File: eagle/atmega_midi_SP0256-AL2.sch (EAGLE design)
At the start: 40 parts, among them IC1 LTC6904, IC2 TL071P, U1 6N138, U2 ATMEGA328P_PDIP, U3 SP0256-AL2

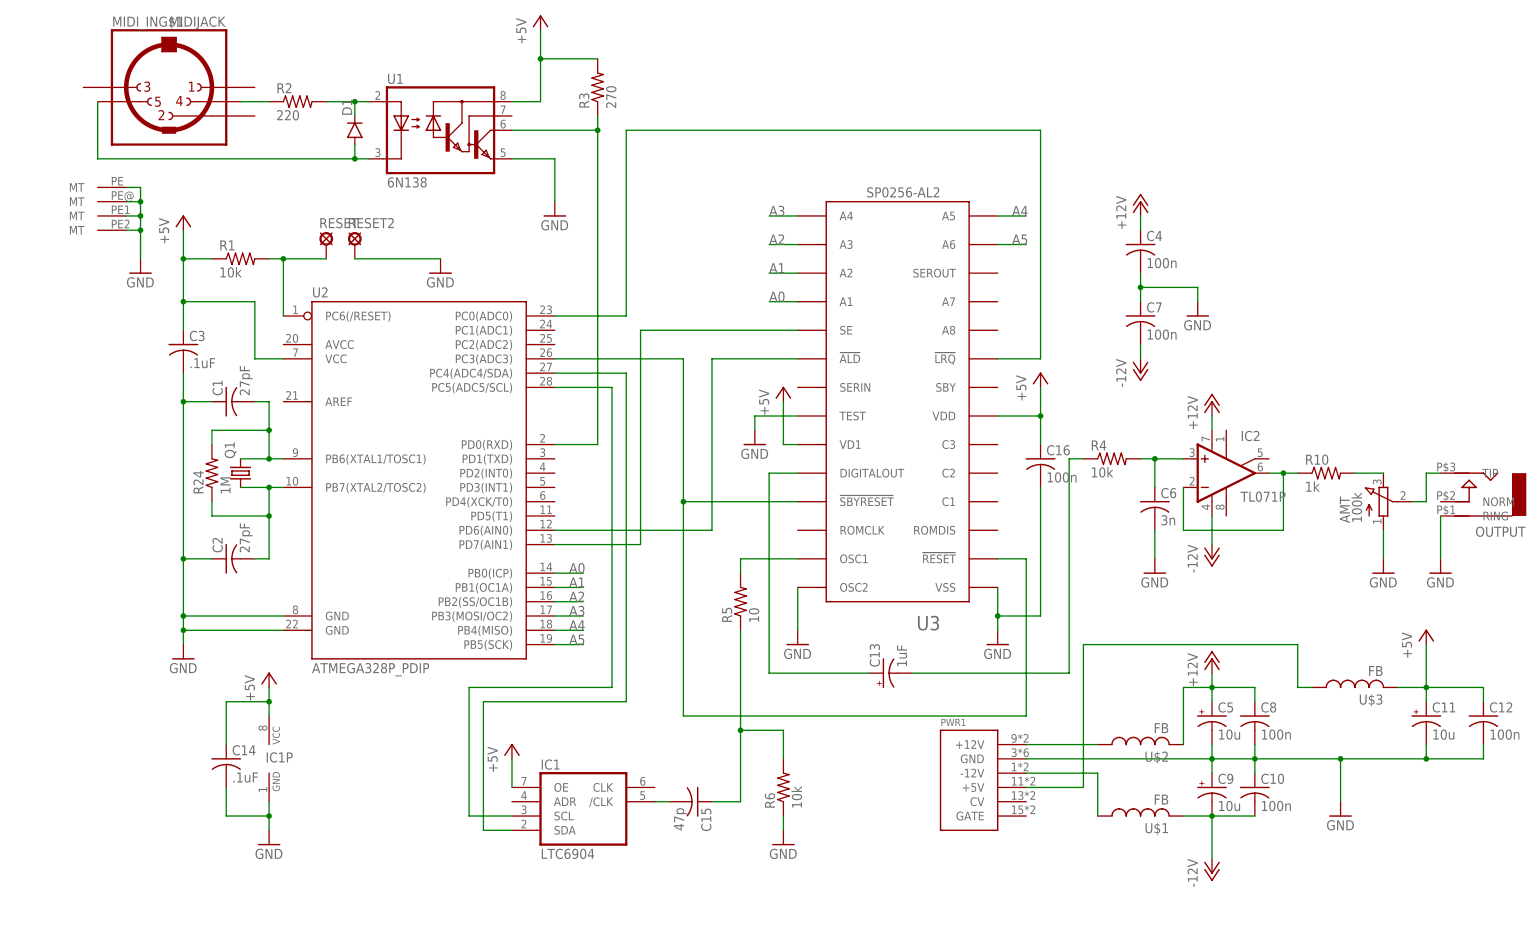
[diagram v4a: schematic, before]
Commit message: routed and stub code for pitch oscillator
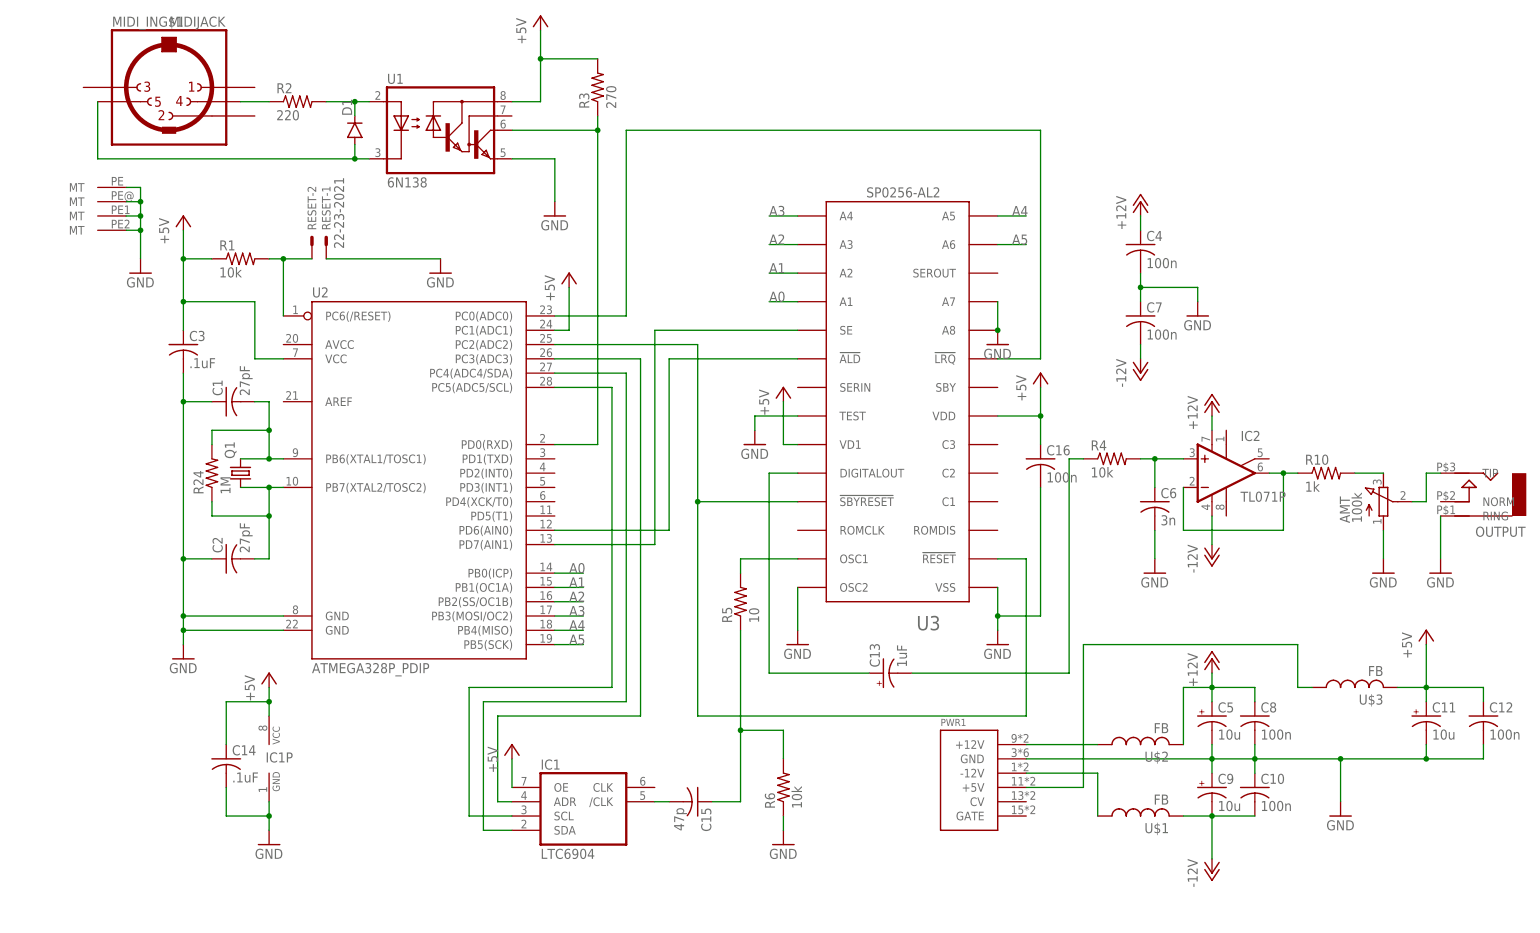
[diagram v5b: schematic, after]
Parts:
- removed RESET2: LSP11, solpad:LSP11
- C13: device rcl:CPOL-USB45181A -> rcl:CPOL-USE15-6AXIAL
- RESET: value LSP11 -> 22-23-2021; device solpad:LSP11 -> con-molex:22-23-2021
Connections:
- new net N$19: IC1G$1.ADR, U2.PC3(ADC3)
- net +5V: now also U2.PC1(ADC1)
- net GND: now also RESET-1.S, U3.A7, U3.A8; no longer RESET2.MP
- net N$1: now also U2.PC2(ADC2); no longer U2.PC3(ADC3)
- net N$43: now also RESET-2.S; no longer RESET.MP
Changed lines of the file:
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@@
 <part name="MIDI_IN" library="adafruit" deviceset="MIDIJACK" device=""/>
 <part name="U3" library="speech" deviceset="SP0256-AL2" device=""/>
-<part name="C13" library="rcl" deviceset="CPOL-US" device="B45181A" value="1uF"/>
+<part name="C13" library="rcl" deviceset="CPOL-US" device="E15-6AXIAL" value="1uF"/>
 <part name="P+3" library="supply1" deviceset="+5V" device=""/>
 <part name="P+6" library="supply1" deviceset="+5V" device=""/>
-<part name="RESET" library="solpad" deviceset="LSP11" device=""/>
-<part name="RESET2" library="solpad" deviceset="LSP11" device=""/>
 <part name="GND12" library="supply1" deviceset="GND" device=""/>
 <part name="GND11" library="supply1" deviceset="GND" device=""/>
@@
 <part name="R6" library="rcl" deviceset="R-US_" device="0207/7" value="10k"/>
 <part name="GND6" library="supply1" deviceset="GND" device=""/>
+<part name="GND10" library="supply1" deviceset="GND" device=""/>
+<part name="P+11" library="supply1" deviceset="+5V" device=""/>
+<part name="RESET" library="con-molex" deviceset="22-23-2021" device=""/>
 </parts>
 <sheets>
@@
 <instance part="P+3" gate="1" x="127" y="63.5"/>
 <instance part="P+6" gate="1" x="81.28" y="60.96"/>
-<instance part="RESET" gate="1" x="0" y="86.36"/>
-<instance part="RESET2" gate="1" x="5.08" y="86.36"/>
 <instance part="MIDI_IN" gate="G$2" x="-35.56" y="96.52" rot="R180"/>
 <instance part="MIDI_IN" gate="G$3" x="-35.56" y="93.98" rot="R180"/>
@@
 <instance part="R6" gate="G$1" x="81.28" y="-10.16" rot="R90"/>
 <instance part="GND6" gate="1" x="81.28" y="-20.32"/>
+<instance part="GND10" gate="1" x="119.38" y="68.58"/>
+<instance part="P+11" gate="1" x="43.18" y="81.28"/>
+<instance part="RESET" gate="-1" x="0" y="86.36" rot="MR90"/>
+<instance part="RESET" gate="-2" x="-2.54" y="86.36" rot="MR90"/>
 </instances>
 <busses>
@@
 <wire x1="33.02" y1="-5.08" x2="33.02" y2="-10.16" width="0.1524" layer="91"/>
 </segment>
+<segment>
+<pinref part="U2" gate="G$1" pin="PC1(ADC1)"/>
+<pinref part="P+11" gate="1" pin="+5V"/>
+<wire x1="40.64" y1="71.12" x2="43.18" y2="71.12" width="0.1524" layer="91"/>
+<wire x1="43.18" y1="71.12" x2="43.18" y2="78.74" width="0.1524" layer="91"/>
+</segment>
 </net>
 <net name="+12V" class="0">
@@
 <segment>
 <pinref part="R1" gate="G$1" pin="2"/>
-<wire x1="0" y1="83.82" x2="-7.62" y2="83.82" width="0.1524" layer="91"/>
+<wire x1="-2.54" y1="83.82" x2="-7.62" y2="83.82" width="0.1524" layer="91"/>
 <pinref part="U2" gate="G$1" pin="PC6(/RESET)"/>
 <wire x1="-7.62" y1="83.82" x2="-10.16" y2="83.82" width="0.1524" layer="91"/>
 <wire x1="-7.62" y1="73.66" x2="-7.62" y2="83.82" width="0.1524" layer="91"/>
 <junction x="-7.62" y="83.82"/>
-<pinref part="RESET" gate="1" pin="MP"/>
+<pinref part="RESET" gate="-2" pin="S"/>
 </segment>
 </net>
@@
 </segment>
 <segment>
-<wire x1="5.08" y1="83.82" x2="20.32" y2="83.82" width="0.1524" layer="91"/>
-<pinref part="RESET2" gate="1" pin="MP"/>
+<wire x1="0" y1="83.82" x2="20.32" y2="83.82" width="0.1524" layer="91"/>
 <pinref part="GND2" gate="1" pin="GND"/>
+<pinref part="RESET" gate="-1" pin="S"/>
 </segment>
 <segment>
@@
 <wire x1="81.28" y1="-17.78" x2="81.28" y2="-15.24" width="0.1524" layer="91"/>
 </segment>
+<segment>
+<pinref part="U3" gate="G$1" pin="A8"/>
+<pinref part="GND10" gate="1" pin="GND"/>
+<pinref part="U3" gate="G$1" pin="A7"/>
+<wire x1="119.38" y1="76.2" x2="119.38" y2="71.12" width="0.1524" layer="91"/>
+<junction x="119.38" y="71.12"/>
+</segment>
 </net>
 <net name="-12V" class="0">
@@
 <net name="N$1" class="0">
 <segment>
-<wire x1="63.5" y1="40.64" x2="63.5" y2="2.54" width="0.1524" layer="91"/>
-<wire x1="63.5" y1="2.54" x2="124.46" y2="2.54" width="0.1524" layer="91"/>
+<wire x1="66.04" y1="40.64" x2="66.04" y2="2.54" width="0.1524" layer="91"/>
+<wire x1="66.04" y1="2.54" x2="124.46" y2="2.54" width="0.1524" layer="91"/>
 <wire x1="124.46" y1="2.54" x2="124.46" y2="30.48" width="0.1524" layer="91"/>
 <pinref part="U3" gate="G$1" pin="!RESET"/>
 <wire x1="124.46" y1="30.48" x2="119.38" y2="30.48" width="0.1524" layer="91"/>
 <pinref part="U3" gate="G$1" pin="!SBYRESET"/>
-<wire x1="83.82" y1="40.64" x2="63.5" y2="40.64" width="0.1524" layer="91"/>
-<wire x1="63.5" y1="40.64" x2="63.5" y2="66.04" width="0.1524" layer="91"/>
-<junction x="63.5" y="40.64"/>
-<pinref part="U2" gate="G$1" pin="PC3(ADC3)"/>
-<wire x1="40.64" y1="66.04" x2="63.5" y2="66.04" width="0.1524" layer="91"/>
+<wire x1="83.82" y1="40.64" x2="66.04" y2="40.64" width="0.1524" layer="91"/>
+<wire x1="66.04" y1="40.64" x2="66.04" y2="68.58" width="0.1524" layer="91"/>
+<junction x="66.04" y="40.64"/>
+<pinref part="U2" gate="G$1" pin="PC2(ADC2)"/>
+<wire x1="40.64" y1="68.58" x2="66.04" y2="68.58" width="0.1524" layer="91"/>
 </segment>
 </net>
@@
 <segment>
 <pinref part="U3" gate="G$1" pin="!ALD"/>
-<wire x1="83.82" y1="66.04" x2="68.58" y2="66.04" width="0.1524" layer="91"/>
+<wire x1="83.82" y1="66.04" x2="60.96" y2="66.04" width="0.1524" layer="91"/>
 <pinref part="U2" gate="G$1" pin="PD6(AIN0)"/>
-<wire x1="40.64" y1="35.56" x2="68.58" y2="35.56" width="0.1524" layer="91"/>
-<wire x1="68.58" y1="35.56" x2="68.58" y2="66.04" width="0.1524" layer="91"/>
+<wire x1="40.64" y1="35.56" x2="60.96" y2="35.56" width="0.1524" layer="91"/>
+<wire x1="60.96" y1="35.56" x2="60.96" y2="66.04" width="0.1524" layer="91"/>
 </segment>
 </net>
@@
 <segment>
 <pinref part="U3" gate="G$1" pin="SE"/>
-<wire x1="83.82" y1="71.12" x2="55.88" y2="71.12" width="0.1524" layer="91"/>
-<wire x1="55.88" y1="71.12" x2="55.88" y2="33.02" width="0.1524" layer="91"/>
+<wire x1="83.82" y1="71.12" x2="58.42" y2="71.12" width="0.1524" layer="91"/>
+<wire x1="58.42" y1="71.12" x2="58.42" y2="33.02" width="0.1524" layer="91"/>
 <pinref part="U2" gate="G$1" pin="PD7(AIN1)"/>
-<wire x1="55.88" y1="33.02" x2="40.64" y2="33.02" width="0.1524" layer="91"/>
-</segment>
-</net>
+<wire x1="58.42" y1="33.02" x2="40.64" y2="33.02" width="0.1524" layer="91"/>
+</segment>
+</net>
+<net name="N$19" class="0">
+<segment>
+<pinref part="U2" gate="G$1" pin="PC3(ADC3)"/>
+<wire x1="40.64" y1="66.04" x2="55.88" y2="66.04" width="0.1524" layer="91"/>
+<wire x1="55.88" y1="66.04" x2="55.88" y2="2.54" width="0.1524" layer="91"/>
+<wire x1="55.88" y1="2.54" x2="30.48" y2="2.54" width="0.1524" layer="91"/>
+<wire x1="30.48" y1="2.54" x2="30.48" y2="-12.7" width="0.1524" layer="91"/>
+<pinref part="IC1" gate="G$1" pin="ADR"/>
+<wire x1="30.48" y1="-12.7" x2="33.02" y2="-12.7" width="0.1524" layer="91"/>
+</segment>
+</net>
